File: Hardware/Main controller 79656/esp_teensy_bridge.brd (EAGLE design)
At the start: 99.8 x 88.1 mm, 93 parts, among them IC2 PBQ79656PAPTQ1, Q5 VISHAY_SIS862DN-T1-GE3VISHAY_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, Q6 VISHAY_SIS862DN-T1-GE3VISHAY_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, Q7 VISHAY_SIS862DN-T1-GE3VISHAY_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, Q8 VISHAY_SIS862DN-T1-GE3VISHAY_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, T2 PBHV8115X, 115, U1 CAN_TRANSCAN_TRANS, U2 ESP32-DEVKITC-32D, U3 CAN_TRANSCAN_TRANS, U4 CAN_TRANSCAN_TRANS, U5 CAN_TRANSCAN_TRANS, X1 5566-12

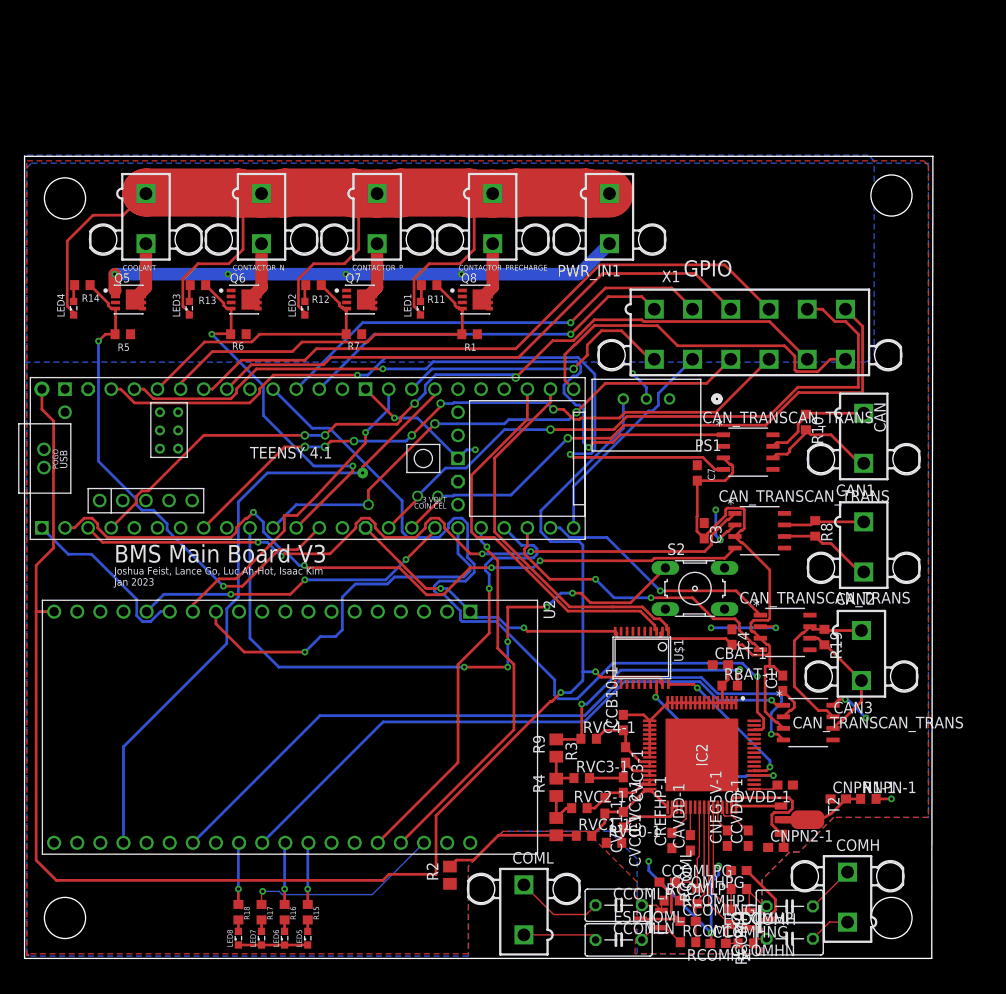
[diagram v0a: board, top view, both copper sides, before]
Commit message: Labelled HV/LV on mainboard
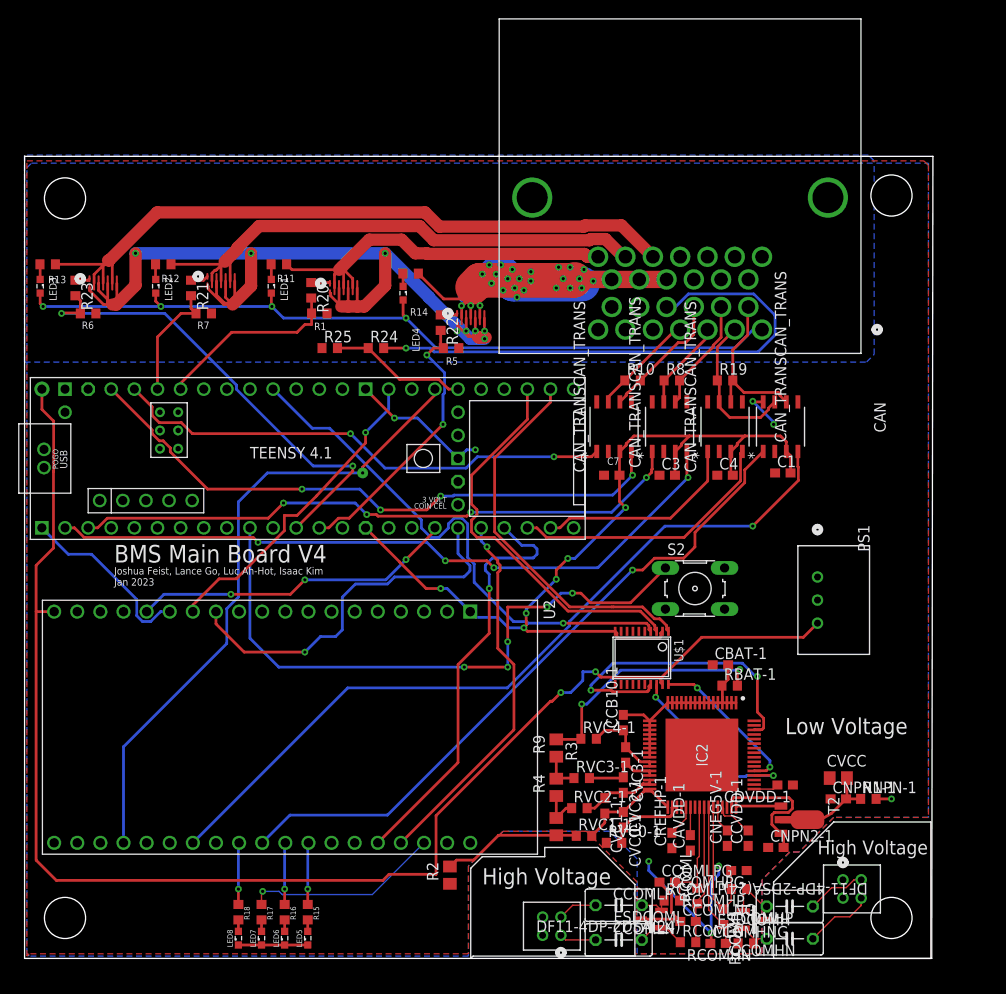
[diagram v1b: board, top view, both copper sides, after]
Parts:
- removed CAN1, CAN2, CAN3, COMH, COML, CONTACTOR_N, CONTACTOR_P, CONTACTOR_PRECHARGE, COOLANT, PWR_IN1: 5566-2, con-molex:5566-2
- removed Q5, Q6, Q7, Q8: VISHAY_SIS862DN-T1-GE3VISHAY_SIS862DN-T1-GE3_0_0, Vishay - SIS862DN-T1-GE3:VISHAY_SIS862DN-T1-GE3_0
- removed X1: 5566-12, con-molex:5566-12
- added CVCC: 10uf, rcl:C0805
- added J1, J2: DF11-4DP-2DSA(24), hirose_connectors:CON4_2X2_UF_DF11_HIR
- added J3: TE_AMP_SURESEAL_26, TE_Sureseal:CONN26_6473423-1_TEC
- added Q1, Q2, Q3, Q4: EPC2065, EPCGaNFET:EPC2065_ECC
- added R20, R21, R22, R23: 300, rcl:R0603
- added R24: 6k, rcl:R0603
- added R25: 1k, rcl:R0603
- moved LED4 36.2 mm to (41.6, 73.1), turned to 270 degrees
- moved R5 36.1 mm to (46.9, 67.1)
- moved R14 36.1 mm to (42.4, 75.2)
- moved U4 32.7 mm to (83.1, 58.4), turned to 90 degrees
- moved R19 30.2 mm to (77.0, 63.5), turned to 0 degrees
- moved PS1 25.4 mm to (87.1, 41.9), turned to 270 degrees
- moved U3 23.6 mm to (77.0, 58.4), turned to 90 degrees
- moved C1 23.1 mm to (83.3, 53.3), turned to 0 degrees
- moved R8 22.6 mm to (71.1, 63.5), turned to 0 degrees
- moved R10 19.6 mm to (66.8, 63.5), turned to 0 degrees
- moved C4 17.8 mm to (77.0, 53.1), turned to 0 degrees
- moved R1 16.7 mm to (32.4, 70.9)
- moved R11 16.7 mm to (27.9, 76.3)
- moved R13 16.7 mm to (2.54, 76.3)
- moved R6 16.7 mm to (6.99, 70.9)
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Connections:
- removed net N$12: CONTACTOR_P.2, Q7.5,6,7,8, Q7.5,6,7,8-2, Q7.5,6,7,8-3, Q7.5,6,7,8-4, Q7.5,6,7,8-5
- removed net N$14: U$3.14-A0/TX3/SPDIF_OUT, X1.1
- removed net N$17: U$3.15-A1/RX3/SPDIF_IN, X1.2
- removed net N$18: U$3.18-A4/SDA0, X1.3
- removed net N$19: U$3.19-A5/SCL0, X1.4
- removed net N$2: CONTACTOR_N.2, Q6.5,6,7,8, Q6.5,6,7,8-2, Q6.5,6,7,8-3, Q6.5,6,7,8-4, Q6.5,6,7,8-5
- removed net N$20: U$3.24-A10/TX6/SCL2, X1.5
- removed net N$21: U$3.25-A11/RX6/SDA2, X1.6
- removed net N$22: U$3.40-A16/CS1, X1.7
- removed net N$23: U$3.32-OUT1B, X1.8
- removed net N$24: U$3.9-OUT1C, X1.9
- removed net N$25: U$3.6-OUT1D, X1.10
- removed net N$26: U$3.33-MCLK2, X1.12
- removed net N$27: U$3.2-OUT2, X1.11
- removed net N$5: COOLANT.2, Q5.5,6,7,8, Q5.5,6,7,8-2, Q5.5,6,7,8-3, Q5.5,6,7,8-4, Q5.5,6,7,8-5
- removed net N$6: CONTACTOR_PRECHARGE.2, Q8.5,6,7,8, Q8.5,6,7,8-2, Q8.5,6,7,8-3, Q8.5,6,7,8-4, Q8.5,6,7,8-5
- new net CONTACTORN_OUT: J3.24, Q3.3, Q3.5, Q3.7, R13.1
- new net CONTACTORPRECHARGE_OUT: J3.26, Q1.3, Q1.5, Q1.7, R11.1
- new net CONTACTORP_OUT: J3.25, Q2.3, Q2.5, Q2.7, R12.1
- new net COOLING_OUT: J3.17, J3.18, J3.19, Q4.3, Q4.5, Q4.7, R14.1
- new net N$15: Q1.1, R20.1
- new net N$16: Q2.1, R21.1
- new net N$30: Q3.1, R23.1
- new net N$36: Q4.1, R22.1
- new net NFAULT_3V3: U$1.4, U$3.16-A2/RX4/SCL1
- new net SHUTDOWN_IN: J3.11, R24.2
- new net SHUTDOWN_SIGNAL: R24.1, R25.2, U$3.38-A14/CS/IN1
- net CANH1: now also J3.4; no longer CAN1.1
- net CANH2: now also J3.3; no longer CAN2.1
- net CANH3: now also J3.2; no longer CAN3.1
- net CANL1: now also J3.10; no longer CAN1.2
- net CANL2: now also J3.9; no longer CAN2.2
- net CANL3: now also J3.8; no longer CAN3.2
- net COMHN: now also J1.4; no longer COMH.1
- net COMHP: now also J1.3; no longer COMH.2
- net COMLN: now also J2.1; no longer COML.1
- net COMLP: now also J2.2; no longer COML.2
- net CONTACTORN_CTRL: now also R23.2; no longer Q6.4, R13.1
- net CONTACTORPRECHARGE_CTRL: now also R20.2; no longer Q8.4, R11.1
- net CONTACTORP_CTRL: now also R21.2; no longer Q7.4, R12.1
- net COOLANT_CTRL: now also R22.2; no longer Q5.4, R14.1
- net GND: now also CVCC.1, J3.12, J3.13, J3.5, J3.6, J3.7, Q1.2, Q1.4, Q1.6, Q1.8, Q2.2, Q2.4, Q2.6, Q2.8, Q3.2, Q3.4, Q3.6, Q3.8, Q4.2, Q4.4, Q4.6, Q4.8, R25.1; no longer PWR_IN1.2, Q5.1, Q5.2, Q5.3, Q6.1, Q6.2, Q6.3, Q7.1, Q7.2, Q7.3, Q8.1, Q8.2, Q8.3
- net N$13: now also LED1.C, R11.2; no longer LED4.A, R14.2
- net N$130: now also CVCC.2
- net N$3: now also LED4.C, R14.2; no longer LED1.A, R11.2
- net N$4: now also LED3.C, R13.2; no longer LED2.A, R12.2
- net N$9: now also LED2.C, R12.2; no longer LED3.A, R13.2
- net NFAULT: now also U$1.17; no longer U$3.16-A2/RX4/SCL1
- net VCC: now also J3.1, LED1.A, LED2.A, LED3.A, LED4.A; no longer CONTACTOR_N.1, CONTACTOR_P.1, CONTACTOR_PRECHARGE.1, COOLANT.1, LED1.C, LED2.C, LED3.C, LED4.C, PWR_IN1.1
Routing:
- net COOLING_OUT: track 0.00 -> 91.7 mm, vias 0 -> 26
- net N$27: track 89.1 -> 0.00 mm, vias 4 -> 0
- net CONTACTORN_OUT: track 0.00 -> 78.0 mm
- net N$25: track 71.5 -> 0.00 mm, vias 6 -> 0
- net N$20: track 70.8 -> 0.00 mm, vias 2 -> 0
- net N$19: track 69.8 -> 0.00 mm
- net N$21: track 66.0 -> 0.00 mm, vias 2 -> 0
- net N$18: track 62.3 -> 0.00 mm
- net CONTACTORP_OUT: track 0.00 -> 59.9 mm
- net SHUTDOWN_IN: track 0.00 -> 59.6 mm, vias 0 -> 1
- net NFAULT: track 94.0 -> 34.7 mm, vias 1 -> 2
- net N$24: track 58.9 -> 0.00 mm, vias 3 -> 0
- net NFAULT_3V3: track 0.00 -> 58.6 mm, vias 0 -> 1
- net N$17: track 49.1 -> 0.00 mm, vias 1 -> 0
- net CONTACTORPRECHARGE_OUT: track 0.00 -> 43.7 mm
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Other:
- board text added: "BMS Main Board V4"
- board text added: "High Voltage"
- board text added: "Low Voltage"
- board text removed: "BMS Main Board V3"
- board text removed: "GPIO"

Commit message: Updates from feedback
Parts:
- added CFET1, CFET2, CFET3, CFET4: 10uf, rcl:C0805
- added R26: 1k, rcl:R0603
- CCOMHN, CCOMHP, CCOMLN, CCOMLP: device rcl:C050-035X075 -> rcl:C075-032X103
- moved J1 5.95 mm to (94.5, 4.83)
- moved J2 2.29 mm to (56.6, 2.54)
- moved CCOMHP 1.52 mm to (85.6, 5.71)
- moved CCOMHN 1.27 mm to (85.3, 2.16)
- moved CCOMLN 1.02 mm to (64.3, 2.03)
- moved CCOMLP 1.02 mm to (64.3, 5.84)
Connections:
- new net N$2: J3.14, R26.2
- net GND: now also CFET1.2, CFET2.1, CFET3.1, CFET4.1
- net SHUTDOWN_IN: now also R26.1
- net VCC: now also CFET1.1, CFET2.2, CFET3.2, CFET4.2
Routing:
- net COOLING_OUT: track 91.7 -> 108.3 mm
- net N$2: track 0.00 -> 12.2 mm
- net VCC: track 117.7 -> 126.6 mm, vias 7 -> 11
- net SHUTDOWN_IN: track 59.6 -> 63.8 mm, vias 1 -> 2
- net N$8: track 3.77 -> 5.09 mm
- net COMHN: track 7.64 -> 8.80 mm
- net CONTACTORPRECHARGE_CTRL: track 20.6 -> 21.7 mm
- net N$1: track 6.23 -> 7.26 mm
- net COMHP: track 6.52 -> 7.48 mm
- net GND: vias 15 -> 24
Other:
- board text added: "COMH"
- board text added: "COML"
- board text added: "CONTACTORN"
- board text added: "CONTACTORP"
- board text added: "CONTACTORPRECHARGE"
- board text added: "COOLING"
- board text added: "Joshua Feist May 2023"
- board text removed: "Joshua Feist, Lance Go, Luc Ah-Hot, Isaac Kim Jan 2023"

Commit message: Changes, gerbers
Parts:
- moved S2 1.24 mm to (74.9, 41.0)
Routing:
- net N$7: track 68.4 -> 69.7 mm
- net COOLING_OUT: track 108.3 -> 107.1 mm
- net NFAULT_3V3: track 58.6 -> 59.3 mm
- net CONTACTORP_OUT: track 59.9 -> 60.4 mm
